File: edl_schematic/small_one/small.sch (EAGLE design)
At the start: 49 parts, among them IC1 TL084D, IC11 TL084D, IC18 TL084D, IC19 TL084D, IC23 TL084D, IC3 TL084D, U3 TLV5610_DW_20, U4 MAX395EWG

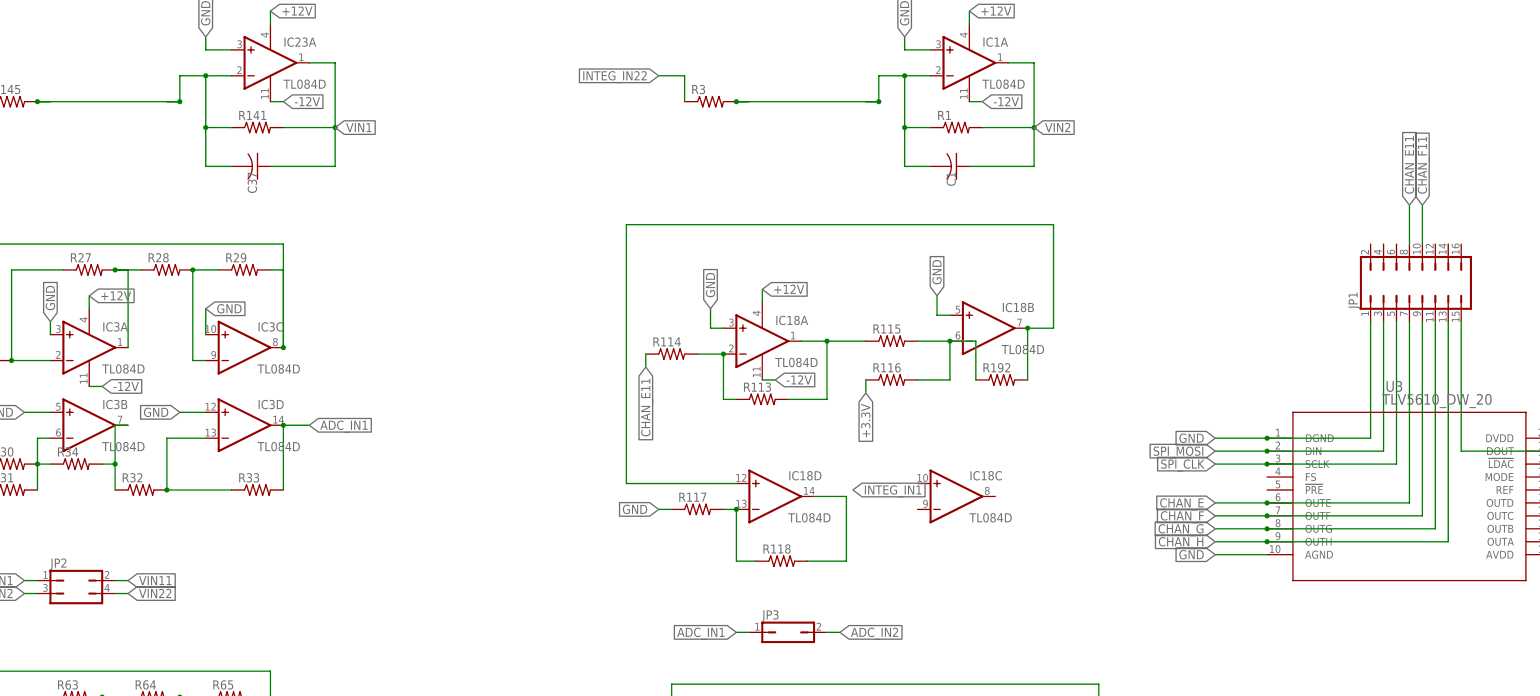
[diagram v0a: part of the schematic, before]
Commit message: Small board done except power and switch
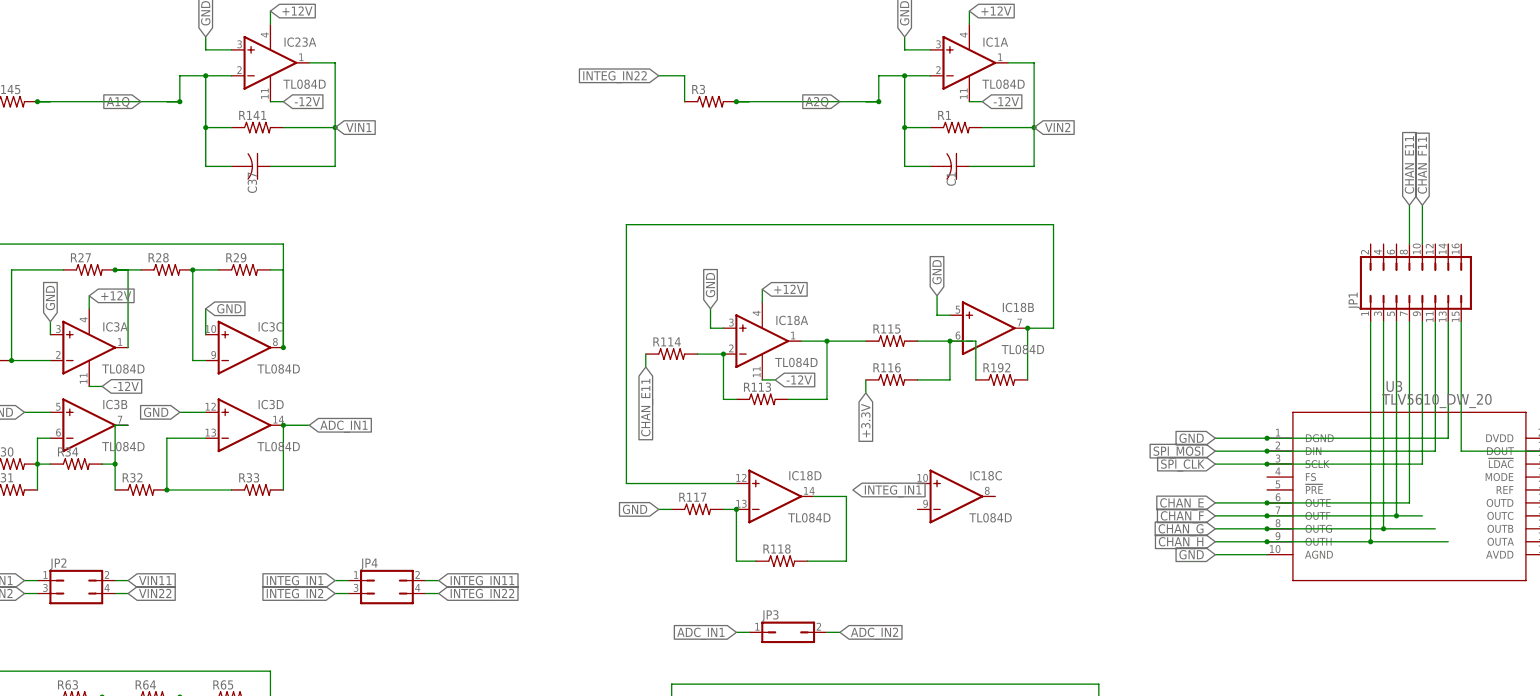
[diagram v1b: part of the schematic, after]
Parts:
- added JP4: (no value), jumper:JP2Q
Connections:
- new net A2Q: C1.2, IC1A.-IN, R1.1, R3.2
- net A1Q: no longer C1.2, IC1A.-IN, R1.1, R3.2
- net CHAN_F: now also JP1.5; no longer JP1.9
- net CHAN_G: now also JP1.3; no longer JP1.11
- net CHAN_H: now also JP1.1; no longer JP1.13
- net GND: now also JP1.13; no longer JP1.1
- net INTEG_IN1: now also JP4.1
- net INTEG_IN11: now also JP4.2
- net INTEG_IN2: now also JP4.3
- net INTEG_IN22: now also JP4.4
- net SPI_CLK: now also JP1.9; no longer JP1.5
- net SPI_MOSI: now also JP1.11; no longer JP1.3

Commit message: small one completed
i guess
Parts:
- added JP5, JP6: (no value), jumper:JP6Q
- added JP7: (no value), jumper:JP2Q
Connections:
- removed net +12V: IC11P.V+, IC18P.V+, IC19P.V+, IC1P.V+, IC23P.V+, IC3P.V+
- removed net +3.3V: R116.1, R122.1, R31.1, R67.1
- removed net -12V: IC11P.V-, IC18P.V-, IC19P.V-, IC1P.V-, IC23P.V-, IC3P.V-
- new net +5V: IC11P.V+, IC18P.V+, IC19P.V+, IC1P.V+, IC23P.V+, IC3P.V+, JP7.1
- new net -5V: IC11P.V-, IC18P.V-, IC19P.V-, IC1P.V-, IC23P.V-, IC3P.V-, JP7.3
- new net A11Q: JP5.11, U4.NO1
- new net FS: JP1.4, U3.FS
- new net LDAC: JP1.6, U3.!LDAC
- new net MODE: JP1.8, U3.MODE
- new net PRE: JP1.2, U3.!PRE
- new net REF: JP1.10, U3.REF
- net 3V3: now also JP5.4, JP6.10, JP7.2, R116.1, R122.1, R31.1, R67.1
- net A1P: now also JP5.9
- net A1Q: no longer U4.NO1
- net A3P: now also JP5.10
- net A3Q: now also JP5.12
- net A5P: now also JP5.1
- net A5Q: now also JP5.3
- net A7P: now also JP5.7
- net A7Q: now also JP5.5
- net B1P: now also JP6.4
- net B1Q: now also JP6.2
- net B3P: now also JP6.3
- net B3Q: now also JP6.1
- net B5P: now also JP6.5
- net B5Q: now also JP6.7
- net B7P: now also JP6.11
- net B7Q: now also JP6.9
- net CHAN_E11: now also JP1.14; no longer JP1.8
- net CHAN_F11: now also JP1.16; no longer JP1.10
- net CS_SW: now also JP6.12
- net GND: now also JP5.8, JP6.6, JP7.4
- net SPI_CLK_SW: now also JP5.2
- net SPI_MOSI_SW: now also JP5.6
- net TO_NEXT1: now also JP6.8
